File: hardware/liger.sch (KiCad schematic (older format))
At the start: 13 parts

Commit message: liger .2
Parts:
- added C? (x3): C, symbol C
- added D?: ZENER, symbol ZENER
- added R?: R, symbol R
- added U1?: SPX3819, symbol SPX3819
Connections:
- net labels added: +5V, EN, Mic_pre-amp, Regulator
- wire segments 23 -> 42
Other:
- moved on the sheet: C?, R?, U?, U?A

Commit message: liger .2
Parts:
- added C?: C, symbol C
- added D?: D, symbol D
- added D? (x2): LED, symbol LED
- added P?: CONN_01X02, symbol CONN_01X02
- added P? (x2): CONN_01X10, symbol CONN_01X10
- added Q?: Q_NPN_BEC, symbol Q_NPN_BEC
- added Q? (x2): Q_NJFET_GSD, symbol Q_NJFET_GSD
- added R? (x8): R, symbol R
- added SW?: SW_PUSH, symbol SW_PUSH
- added U?: FT230XS, SSOP-16, symbol FT230XS
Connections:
- net +3V3: now also D?.2 (A), D?.2 (A), R?.1
- net +5V: now also P?.1 (VCC)
- net EN: no longer U?.2 (EN)
- net GND: now also P?.5 (GND), P?.6 (shield), U?.18 (GND), C?.2, Q?.2 (E), Q?.2 (S), R?.2, SW?.2
- net at Relay?.1: now also D?.2 (A), Q?.3 (C)
- net at Relay?.16: now also D?.1 (K)
- net at Relay?.6: now also P?.2 (P2)
- net at Relay?.9: now also P?.1 (P1)
- net DM: now reaches P?.2 (D-)
- net DP: now reaches P?.3 (D+)
- net at U?.1 (3V3): now also R?.1
- new net: R?.2, U?.2 (EN)
- new net: Q?.1 (B), R?.1
- new net: D?.1 (K), R?.1
- new net: D?.1 (K), Q?.2 (S), R?.1
- new net: Q?.3 (D), R?.2
- new net: Q?.3 (D), R?.1
- new net: C?.1, Q?.1 (G), R?.2
- new net IO0: R?.1
- new net IO15: R?.1, R?.2
- new net IO2: R?.2
- new net IO5: R?.2
- new net Reset: Q?.1 (G), R?.2, SW?.1
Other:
- moved on the sheet: P?, Relay?, U?

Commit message: liger 0.2
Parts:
- U?: footprint (none) -> garage-opener:ESP-WROOM-02; Part Number (none) -> ESP-WROOM-02
- U?: footprint SSOP-16 -> Housings_SSOP:SSOP-16_3.9x4.9mm_Pitch0.635mm; Part Number (none) -> FT230XS
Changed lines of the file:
@@
 F 0 "U?" H 5450 2150 60  0000 C CNN
 F 1 "ESP-WROOM-02" H 5100 3300 60  0000 C CNN
-F 2 "" H 4400 3450 60  0000 C CNN
-F 3 "" H 4400 3450 60  0000 C CNN
+F 2 "garage-opener:ESP-WROOM-02" H 4400 3450 60  0001 C CNN
+F 3 "http://akizukidenshi.com/download/ds/espressifsystems/0C-ESP8266__WROOM_WiFi_Module_Datasheet__EN_v0.3.pdf" H 4400 3450 60  0001 C CNN
+F 4 "ESP-WROOM-02" H 4400 3450 60  0001 C CNN "Part Number"
 	1    4400 3450
 	1    0    0    -1
@@
 F 0 "U?" H 6500 4750 50  0000 L CNN
 F 1 "FT230XS" H 7350 4750 50  0000 L CNN
-F 2 "SSOP-16" H 7050 4150 50  0000 C CNN
-F 3 "" H 7050 4150 50  0000 C CNN
+F 2 "Housings_SSOP:SSOP-16_3.9x4.9mm_Pitch0.635mm" H 7050 4150 50  0001 C CNN
+F 3 "http://www.mouser.com/ds/2/163/DS_FT230X-5395.pdf" H 7050 4150 50  0001 C CNN
+F 4 "FT230XS" H 7050 4150 60  0001 C CNN "Part Number"
 	1    7050 4150
 	1    0    0    -1

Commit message: update
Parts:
- added C? (x3): C, symbol C
- added D? (x3): LED, symbol LED
- added FB?: BK0603HS330-T, symbol BK0603HS330-T
- added R? (x6): R, symbol R
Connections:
- net +3V3: now also FB?.1
- net DM: now also C?.1, R?.2
- net DP: now also C?.1, R?.2
- net GND: now also U?.13 (GND), U?.5 (GND), C?.2, C?.2, C?.2
- net RXD: now reaches U?.1 (TXD)
- net at U?.10 (3V3OUT): now also U?.11 (~RESET), U?.3 (VCCIO), C?.1, D?.2 (A), D?.2 (A), D?.2 (A)
- net at U?.12 (VCC): now also FB?.2
- net at U?.14 (CBUS1): now also R?.2
- net at U?.15 (CBUS0): now also R?.2
- net at U?.16 (CBUS3): now also R?.2
- net TXD: now reaches U?.4 (RXD)
- net at U?.7 (CBUS2): now also R?.2
- net at U?.8 (USBDP): now also R?.1
- net at U?.9 (USBDM): now also R?.1
- new net: D?.1 (K), R?.1 (x3)
- new net RESET: R?.1
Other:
- moved on the sheet: U?

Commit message: update
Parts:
- removed C?: C, symbol C
- removed Q? (x2): Q_NJFET_GSD, symbol Q_NJFET_GSD
- removed R? (x15): R, symbol R
- added C?: 47 pF, Capacitors_SMD:C_0402, symbol C
- added Q?: Q_PMOS_GSD, symbol Q_PMOS_GSD
- added Q?: Q_NMOS_GSD, symbol Q_NMOS_GSD
- added R? (x10): 1K, Resistors_SMD:R_0603, symbol R
- added R? (x4): 10K, Resistors_SMD:R_0603, symbol R
- added R?: 27K, Resistors_SMD:R_0603, symbol R
- C?: value C -> 3.7uF
- C?: value C -> 10uF
- C?: value C -> 0.1uf
- C? (x2): value C -> 1uf
- C?: value C -> 4.7uF
- C?: value C -> 47 pF; footprint (none) -> Capacitors_SMD:C_0402; Part Number (none) -> GRM1555C1H470FA01D
- C?: value C -> 100nF
- R?: value R -> 2.2K; footprint (none) -> Resistors_SMD:R_0603; Part Number (none) -> RC0603FR-072K2L
- R?: value R -> 1M
- R?: value R -> 10K; footprint (none) -> Resistors_SMD:R_0603; Part Number (none) -> RC0603JR-0710KL
- R?: value R -> 1K; footprint (none) -> Resistors_SMD:R_0603; Part Number (none) -> RC0603JR-071KL
- R?: value R -> 27K; footprint (none) -> Resistors_SMD:R_0603; Part Number (none) -> ERJ-3GEYJ273V
- gave numbers to parts that had none: 1
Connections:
- net +3V3: now also R?.2
- net DM: now also C?.1, R?.2
- net GND: now also C?.2, Q?.2 (S), R?.1, R?.1, R?.2
- net IO0: now also R?.1
- net IO15: now also R?.1, R?.2
- net IO5: now also R?.2
- net RESET: now also R?.1
- net Reset: now also Q?.1 (G), R?.2
- net at U?.1 (3V3): now also R?.2
- net at U?.2 (EN): now also R?.1
- net at R?.2, U?.1 (+): now also C?.1; no longer C?.2
- net at R?.2: now also C?.2; no longer C?.1
- net at C?.1, U?.2 (-): now also R?.1, R?.2
- net at C?.1, D?.1 (K), U1?.1 (IN)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: now also R?.2
- net at Q?.1 (B): now also R?.1
- net at U?.14 (CBUS1): now also R?.2
- net at U?.15 (CBUS0): now also R?.2
- net at U?.16 (CBUS3): now also R?.2
- net at U?.7 (CBUS2): now also R?.2
- net at U?.9 (USBDM): now also R?.1
- net at D?.1 (K): now also R?.1 (x4)
- net at D?.1 (K): now also Q?.2 (S), R?.1
- net at C?.1: now also Q?.1 (G), R?.2
- new net: Q?.3 (D), R?.1
- new net: Q?.3 (D), R?.2
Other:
- moved on the sheet: C?, D?, FB?, P?, R?, U?

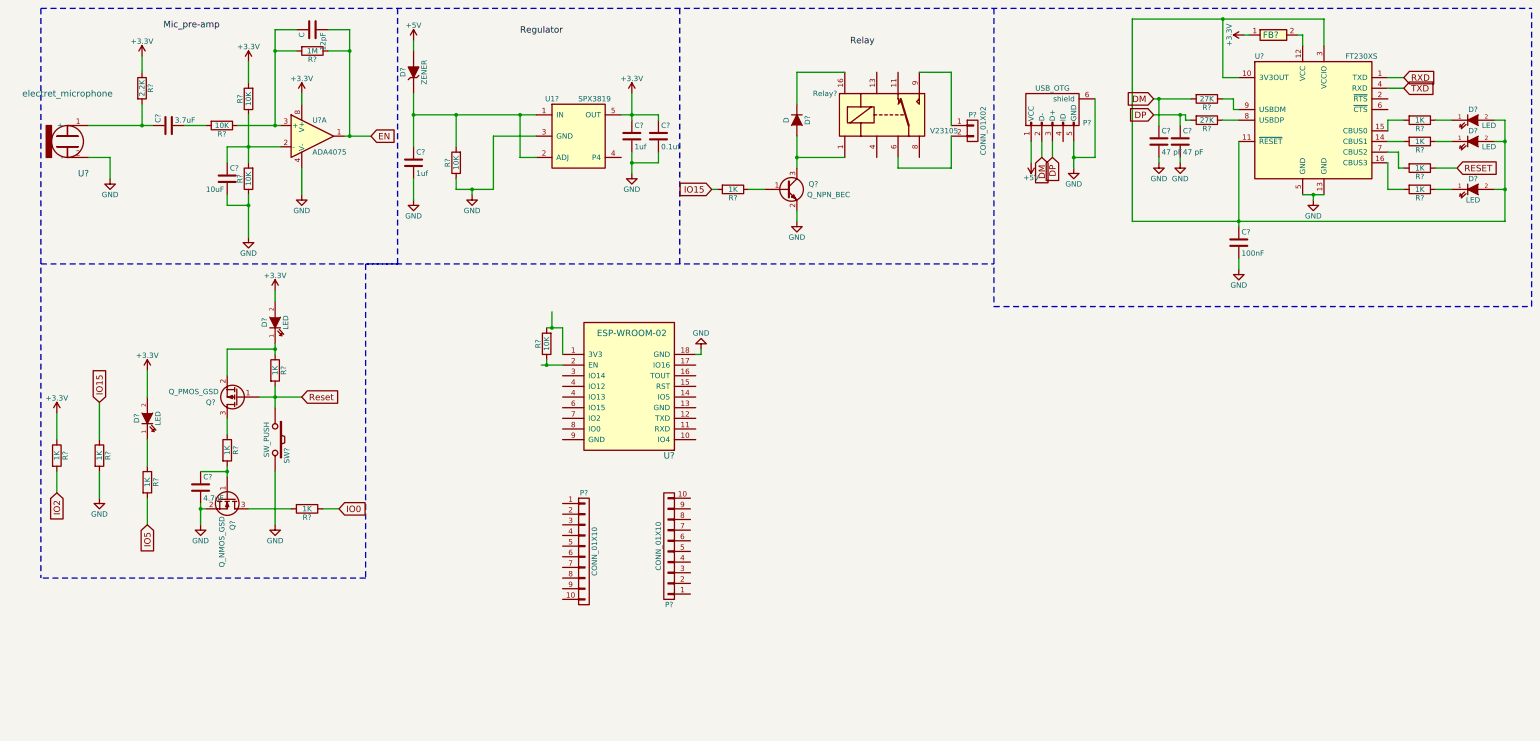
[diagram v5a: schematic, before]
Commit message: more datasheets
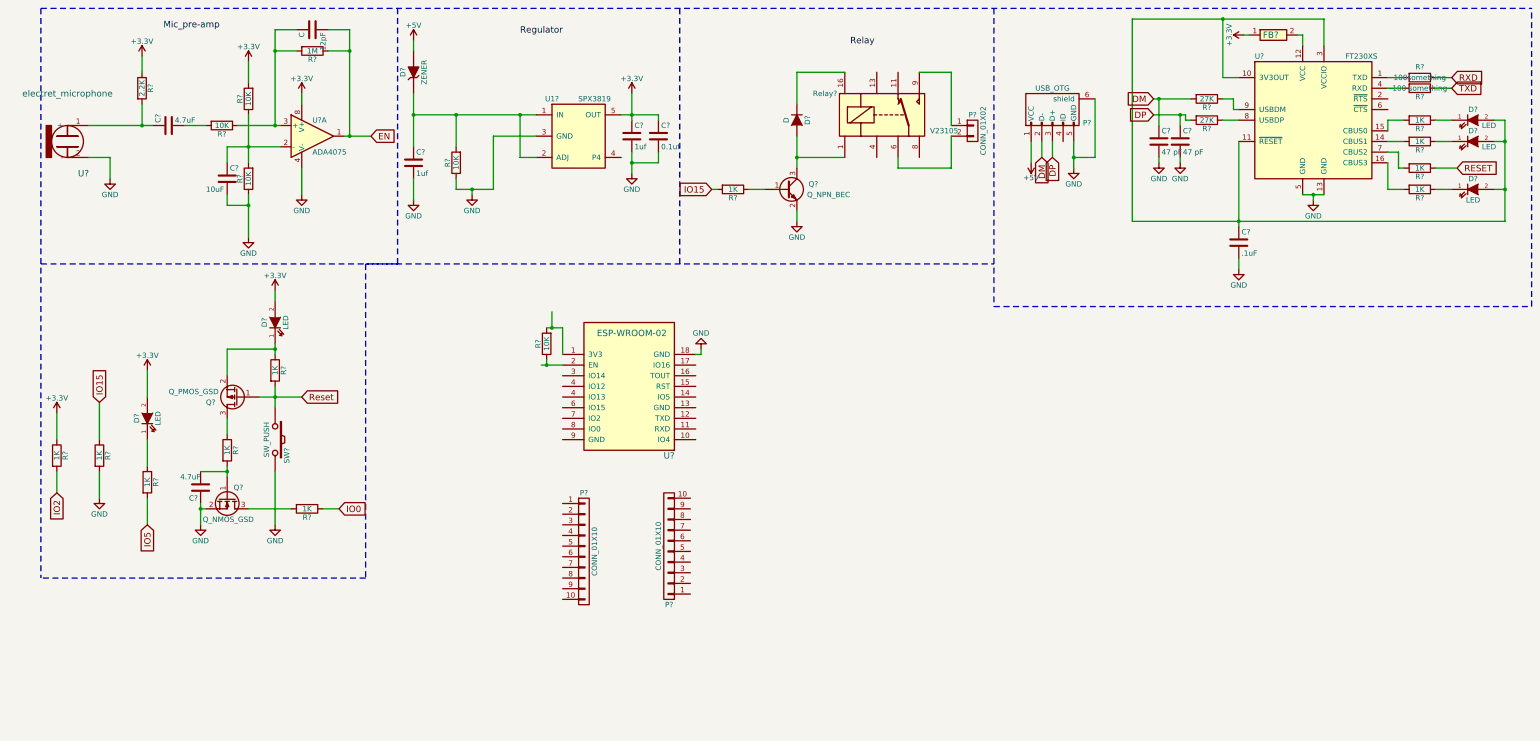
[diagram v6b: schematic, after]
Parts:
- removed C?: 1uf, symbol C
- removed C?: 4.7uF, symbol C
- added C?: 1uf, Capacitors_SMD:C_0603, symbol C
- added C?: 4.7uF, Capacitors_SMD:C_0603, symbol C
- added R?: 100something, symbol R
- added R?: 100 something, symbol R
- 12pF: footprint (none) -> Capacitors_SMD:C_0402; Part Number (none) -> C0402C120J5GACTU
- C?: value 3.7uF -> 4.7uF; footprint (none) -> Capacitors_SMD:C_0603; Part Number (none) -> CL10B475KQ8NQNC
- C?: footprint (none) -> Capacitors_SMD:C_0603; Part Number (none) -> GRM188R60G106ME47D
- C?: footprint (none) -> Capacitors_SMD:C_0201; Part Number (none) -> GRM0335C1ER10BA01D
- C?: footprint (none) -> Capacitors_SMD:C_0603; Part Number (none) -> CC0603ZRY5V7BB105
- C?: value 100nF -> .1uF; footprint (none) -> Capacitors_SMD:C_0603; Part Number (none) -> CC0603ZRY5V9BB104
- D?: footprint (none) -> Diodes_SMD:SOD-123; Part Number (none) -> MBR120VLSFT1G
- D?: footprint (none) -> Diodes_SMD:SMA_Standard; Part Number (none) -> SS14
- Q?: footprint (none) -> TO_SOT_Packages_SMD:SOT-23; Part Number (none) -> MMBT3904LT1G
- Q?: footprint (none) -> TO_SOT_Packages_SMD:SOT-23; Part Number (none) -> BSS84LT1G
- Q?: footprint (none) -> TO_SOT_Packages_SMD:SOT-23; Part Number (none) -> 2N7002L
- U1?: footprint (none) -> TO_SOT_Packages_SMD:SOT-23-5; Part Number (none) -> SPX3819
- U?: footprint (none) -> Housings_SOIC:SOIC-8_3.9x4.9mm_Pitch1.27mm; Part Number (none) -> OPA344NA/3K
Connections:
- net +3V3: now also C?.1
- net GND: now also C?.1, C?.2
- net RXD: now also R?.1; no longer U?.1 (TXD)
- net TXD: now also R?.1; no longer U?.4 (RXD)
- net at Q?.1 (G), R?.2: now also C?.2
- new net: R?.2, U?.1 (TXD)
- new net: R?.2, U?.4 (RXD)
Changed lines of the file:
@@
 P 1700 1650
 F 0 "C?" H 1725 1750 50  0000 L CNN
-F 1 "3.7uF" V 1750 1400 50  0000 L CNN
-F 2 "" H 1738 1500 50  0000 C CNN
-F 3 "" H 1700 1650 50  0000 C CNN
+F 1 "4.7uF" V 1750 1400 50  0000 L CNN
+F 2 "Capacitors_SMD:C_0603" H 1738 1500 50  0001 C CNN
+F 3 "http://media.digikey.com/pdf/Data%20Sheets/Samsung%20PDFs/CL_Series_MLCC_ds.pdf" H 1700 1650 50  0001 C CNN
+F 4 "CL10B475KQ8NQNC" H 1700 1650 60  0001 C CNN "Part Number"
 	1    1700 1650
 	0    -1   -1   0
@@
 F 0 "C?" H 2275 2250 50  0000 L CNN
 F 1 "10uF" H 2050 2050 50  0000 L CNN
-F 2 "" H 2288 2000 50  0000 C CNN
-F 3 "" H 2250 2150 50  0000 C CNN
+F 2 "Capacitors_SMD:C_0603" H 2288 2000 50  0001 C CNN
+F 3 "http://www.murata.com/~/media/webrenewal/support/library/catalog/products/capacitor/mlcc/c02e.pdf" H 2250 2150 50  0001 C CNN
+F 4 "GRM188R60G106ME47D" H 2250 2150 60  0001 C CNN "Part Number"
 	1    2250 2150
 	1    0    0    -1
@@
 F 0 "12pF" H 3075 850 50  0000 L CNN
 F 1 "C" H 3075 650 50  0000 L CNN
-F 2 "" H 3088 600 50  0000 C CNN
-F 3 "" H 3050 750 50  0000 C CNN
+F 2 "Capacitors_SMD:C_0402" H 3088 600 50  0001 C CNN
+F 3 "http://www.kemet.com/Lists/ProductCatalog/Attachments/46/KEM_C1003_C0G_SMD.pdf" H 3050 750 50  0001 C CNN
+F 4 "C0402C120J5GACTU" H 3050 750 60  0001 C CNN "Part Number"
 	1    3050 750
 	0    1    1    0
@@
 F 0 "U?" H 3050 1900 50  0000 L CNN
 F 1 "ADA4075" H 3050 1600 50  0000 L CNN
-F 2 "" H 2950 1800 50  0000 C CNN
-F 3 "" H 3050 1900 50  0000 C CNN
+F 2 "Housings_SOIC:SOIC-8_3.9x4.9mm_Pitch1.27mm" H 2950 1800 50  0001 C CNN
+F 3 "http://www.mouser.com/ds/2/609/OP275-879536.pdf" H 3050 1900 50  0001 C CNN
+F 4 "OPA344NA/3K" H 3050 1750 60  0001 C CNN "Part Number"
 	1    3050 1750
 	1    0    0    -1
@@
 F 0 "U1?" H 5300 2100 50  0000 C CNN
 F 1 "SPX3819" H 5700 2100 50  0000 C CNN
-F 2 "" H 5550 1350 50  0000 C CIN
-F 3 "" H 5600 1250 50  0001 C CNN
+F 2 "TO_SOT_Packages_SMD:SOT-23-5" H 5550 1350 50  0001 C CIN
+F 3 "http://www.mouser.com/ds/2/146/SPX3819_DS_R200_082312-17072.pdf" H 5600 1250 50  0001 C CNN
+F 4 "SPX3819" H 5550 1750 60  0001 C CNN "Part Number"
 	1    5550 1750
 	1    0    0    -1
@@
 F 0 "C?" H 6325 1850 50  0000 L CNN
 F 1 "0.1uf" H 6325 1650 50  0000 L CNN
-F 2 "" H 6338 1600 50  0000 C CNN
-F 3 "" H 6300 1750 50  0000 C CNN
+F 2 "Capacitors_SMD:C_0201" H 6338 1600 50  0001 C CNN
+F 3 "http://www.murata.com/~/media/webrenewal/support/library/catalog/products/capacitor/mlcc/c02e.pdf" H 6300 1750 50  0001 C CNN
+F 4 "GRM0335C1ER10BA01D" H 6300 1750 60  0001 C CNN "Part Number"
 	1    6300 1750
-	1    0    0    -1
-$EndComp
-$Comp
-L C C?
-U 1 1 57682424
-P 6050 1750
-F 0 "C?" H 6075 1850 50  0000 L CNN
-F 1 "1uf" H 6075 1650 50  0000 L CNN
-F 2 "" H 6088 1600 50  0000 C CNN
-F 3 "" H 6050 1750 50  0000 C CNN
-	1    6050 1750
 	1    0    0    -1
 $EndComp
@@
 F 0 "D?" H 4000 1250 50  0000 C CNN
 F 1 "ZENER" H 4000 1050 50  0000 C CNN
-F 2 "" H 4000 1150 50  0000 C CNN
-F 3 "" H 4000 1150 50  0000 C CNN
+F 2 "Diodes_SMD:SOD-123" H 4000 1150 50  0001 C CNN
+F 3 "http://www.mouser.com/ds/2/308/MBR120VLSFT1-D-107081.pdf" H 4000 1150 50  0001 C CNN
+F 4 "MBR120VLSFT1G" H 4000 1150 60  0001 C CNN "Part Number"
 	1    4000 1150
 	0    -1   -1   0
@@
 F 0 "C?" H 4025 2100 50  0000 L CNN
 F 1 "1uf" H 4025 1900 50  0000 L CNN
-F 2 "" H 4038 1850 50  0000 C CNN
-F 3 "" H 4000 2000 50  0000 C CNN
+F 2 "Capacitors_SMD:C_0603" H 4038 1850 50  0001 C CNN
+F 3 "http://www.yageo.com/documents/recent/UPY-GPHC_Y5V_6.3V-to-50V_6.pdf" H 4000 2000 50  0001 C CNN
+F 4 "CC0603ZRY5V7BB105" H 4000 2000 60  0001 C CNN "Part Number"
 	1    4000 2000
 	1    0    0    -1
@@
 F 0 "D?" H 7600 1700 50  0000 C CNN
 F 1 "D" H 7600 1500 50  0000 C CNN
-F 2 "" H 7600 1600 50  0000 C CNN
-F 3 "" H 7600 1600 50  0000 C CNN
+F 2 "Diodes_SMD:SMA_Standard" H 7600 1600 50  0001 C CNN
+F 3 "http://www.mouser.com/ds/2/149/BAT54-888471.pdf" H 7600 1600 50  0001 C CNN
+F 4 "SS14" H 7600 1600 60  0001 C CNN "Part Number"
 	1    7600 1600
 	0    1    1    0
@@
 F 0 "Q?" H 7800 2300 50  0000 R CNN
 F 1 "Q_NPN_BEC" H 8100 2200 50  0000 R CNN
-F 2 "" H 7700 2350 50  0000 C CNN
-F 3 "" H 7500 2250 50  0000 C CNN
+F 2 "TO_SOT_Packages_SMD:SOT-23" H 7700 2350 50  0001 C CNN
+F 3 "http://www.mouser.com/ds/2/308/MMBT3904LT1-D-113169.pdf" H 7500 2250 50  0001 C CNN
+F 4 "MMBT3904LT1G" H 7500 2250 60  0001 C CNN "Part Number"
 	1    7500 2250
 	1    0    0    -1
@@
 	2250 4850 2250 4950
 Connection ~ 2250 4900
-$Comp
-L C C?
-U 1 1 5768BDFE
-P 2000 5050
-F 0 "C?" H 2025 5150 50  0000 L CNN
-F 1 "4.7uF" H 2025 4950 50  0000 L CNN
-F 2 "" H 2038 4900 50  0000 C CNN
-F 3 "" H 2000 5050 50  0000 C CNN
-	1    2000 5050
-	1    0    0    -1
-$EndComp
 Wire Wire Line
 	2050 5250 2000 5250
@@
 Text GLabel 13800 2050 2    60   Input ~ 0
 RESET
-Text GLabel 13300 1300 2    60   Input ~ 0
+Text GLabel 13750 1300 2    60   Input ~ 0
 TXD
-Text GLabel 13300 1200 2    60   Input ~ 0
+Text GLabel 13750 1200 2    60   Input ~ 0
 RXD
 Wire Wire Line
@@
 P 11750 2750
 F 0 "C?" H 11775 2850 50  0000 L CNN
-F 1 "100nF" H 11775 2650 50  0000 L CNN
-F 2 "" H 11788 2600 50  0000 C CNN
-F 3 "" H 11750 2750 50  0000 C CNN
+F 1 ".1uF" H 11775 2650 50  0000 L CNN
+F 2 "Capacitors_SMD:C_0603" H 11788 2600 50  0001 C CNN
+F 3 "http://www.yageo.com/documents/recent/UPY-GPHC_Y5V_6.3V-to-50V_6.pdf" H 11750 2750 50  0001 C CNN
+F 4 "CC0603ZRY5V9BB104" H 11750 2750 60  0001 C CNN "Part Number"
 	1    11750 2750
 	1    0    0    -1
@@
 F 0 "Q?" H 2650 4250 50  0000 R CNN
 F 1 "Q_PMOS_GSD" H 3000 4150 50  0000 R CNN
-F 2 "" H 2550 4300 50  0000 C CNN
-F 3 "" H 2350 4200 50  0000 C CNN
+F 2 "TO_SOT_Packages_SMD:SOT-23" H 2550 4300 50  0001 C CNN
+F 3 "http://www.mouser.com/ds/2/308/BSS84LT1-D-105913.pdf" H 2350 4200 50  0001 C CNN
+F 4 "BSS84LT1G" H 2350 4200 60  0001 C CNN "Part Number"
 	1    2350 4200
 	-1   0    0    1
@@
 U 1 1 576D6F9D
 P 2250 5150
-F 0 "Q?" H 2550 5200 50  0000 R CNN
-F 1 "Q_NMOS_GSD" H 2900 5100 50  0000 R CNN
-F 2 "" H 2450 5250 50  0000 C CNN
-F 3 "" H 2250 5150 50  0000 C CNN
+F 0 "Q?" V 2150 5300 50  0000 R CNN
+F 1 "Q_NMOS_GSD" V 2450 5400 50  0000 R CNN
+F 2 "TO_SOT_Packages_SMD:SOT-23" H 2450 5250 50  0001 C CNN
+F 3 "http://www.mouser.com/ds/2/308/2N7002L-D-105484.pdf" H 2250 5150 50  0001 C CNN
+F 4 "2N7002L" V 2250 5150 60  0001 C CNN "Part Number"
 	1    2250 5150
 	0    1    1    0
@@
 	1    0    0    -1
 $EndComp
+$Comp
+L C C?
+U 1 1 576FFA59
+P 6050 1750
+F 0 "C?" H 6075 1850 50  0000 L CNN
+F 1 "1uf" H 6075 1650 50  0000 L CNN
+F 2 "Capacitors_SMD:C_0603" H 6088 1600 50  0001 C CNN
+F 3 "http://www.yageo.com/documents/recent/UPY-GPHC_Y5V_6.3V-to-50V_6.pdf" H 6050 1750 50  0001 C CNN
+F 4 "CC0603ZRY5V7BB105" H 6050 1750 60  0001 C CNN "Part Number"
+	1    6050 1750
+	1    0    0    -1
+$EndComp
+$Comp
+L R R?
+U 1 1 57701A9A
+P 13450 1200
+F 0 "R?" V 13350 1200 50  0000 C CNN
+F 1 "100something" V 13450 1200 50  0000 C CNN
+F 2 "" V 13380 1200 50  0000 C CNN
+F 3 "" H 13450 1200 50  0000 C CNN
+	1    13450 1200
+	0    1    1    0
+$EndComp
+$Comp
+L R R?
+U 1 1 57701B37
+P 13450 1300
+F 0 "R?" V 13530 1300 50  0000 C CNN
+F 1 "100 something" V 13450 1300 50  0000 C CNN
+F 2 "" V 13380 1300 50  0000 C CNN
+F 3 "" H 13450 1300 50  0000 C CNN
+	1    13450 1300
+	0    1    1    0
+$EndComp
+Wire Wire Line
+	13600 1200 13750 1200
+Wire Wire Line
+	13600 1300 13750 1300
+$Comp
+L C C?
+U 1 1 577082C5
+P 2000 5050
+F 0 "C?" H 2025 5150 50  0000 L CNN
+F 1 "4.7uF" H 2000 4950 50  0000 L CNN
+F 2 "Capacitors_SMD:C_0603" H 2038 4900 50  0001 C CNN
+F 3 "http://media.digikey.com/pdf/Data%20Sheets/Samsung%20PDFs/CL_Series_MLCC_ds.pdf" H 2000 5050 50  0001 C CNN
+F 4 "CL10B475KQ8NQNC" H 2000 5050 60  0001 C CNN "Part Number"
+	1    2000 5050
+	-1   0    0    1
+$EndComp
 $EndSCHEMATC
